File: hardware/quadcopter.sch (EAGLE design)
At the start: 92 parts, among them J1 HEADER-4POS-0.1IN-FEMALE-SMD-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, J2 HEADER-10POSTH-254X10, J3 HEADER-4POS-0.1IN-FEMALE, J4 AVR_SPI_PRG_6-SMD, M1 MOTOR_PADS_GND-MOLEX-SMD, M2 MOTOR_PADS_GND-MOLEX-SMD, M3 MOTOR_PADS_GND-MOLEX-SMD, M4 MOTOR_PADS_GND-MOLEX-SMD, Q1 N-MOSFET-SI2302DS, Q10 N-MOSFET-SI2302DS, Q11 N-MOSFET-SI2302DS, Q12 N-MOSFET-SI2302DS, Q2 N-MOSFET-SI2302DS, Q3 N-MOSFET-SI2302DS, Q4 N-MOSFET-SI2302DS, Q5 N-MOSFET-SI2302DS, Q6 N-MOSFET-SI2302DS, Q7 N-MOSFET-SI2302DS, Q8 N-MOSFET-SI2302DS, Q9 N-MOSFET-SI2302DS, SW1 PUSHBUTTON_-4.5X4.5, U1 ATMEGA128RFA1, U2 IMU_LSM9DS1-LSM9DS1, Y1 CRYSTAL5X3

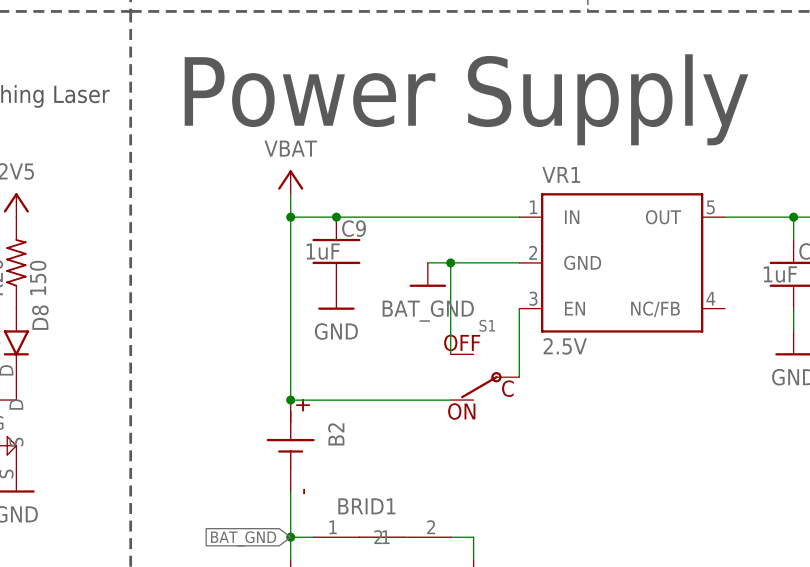
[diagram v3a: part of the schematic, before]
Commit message: Wire decoupling cap between VBAT and BAT_GND
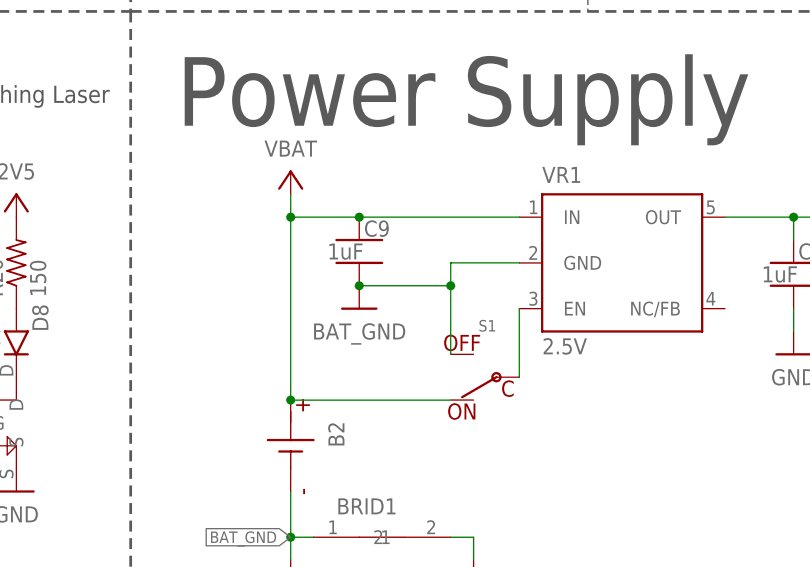
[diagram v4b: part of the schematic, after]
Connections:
- net BAT_GND: now also C9.2
- net GND: no longer C9.2
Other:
- moved on the sheet: C9
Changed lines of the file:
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@@
 <part name="C10" library="quadparts_prebuilt_2022" library_urn="urn:adsk.wipprod:fs.file:vf.VudH_-qgS-enOFMGlZoxrw" deviceset="CAPACITOR-NP_" device="SMD-2012-0805_CERAMIC-1UF" value="1uF"/>
 <part name="S1" library="quadparts_prebuilt_2022" library_urn="urn:adsk.wipprod:fs.file:vf.VudH_-qgS-enOFMGlZoxrw" deviceset="POWER-SWITCH-MFS201N-9-Z" device="-SMD-EDGE"/>
-<part name="GND31" library="quadparts_prebuilt_2022" library_urn="urn:adsk.wipprod:fs.file:vf.VudH_-qgS-enOFMGlZoxrw" deviceset="GND" device=""/>
 <part name="GND33" library="quadparts_prebuilt_2022" library_urn="urn:adsk.wipprod:fs.file:vf.VudH_-qgS-enOFMGlZoxrw" deviceset="GND" device=""/>
 <part name="GND32" library="quadparts_prebuilt_2022" library_urn="urn:adsk.wipprod:fs.file:vf.VudH_-qgS-enOFMGlZoxrw" deviceset="BAT_GND" device=""/>
@@
 <attribute name="NAME" x="373.38" y="110.49" size="1.778" layer="95"/>
 </instance>
-<instance part="C9" gate="G$1" x="350.52" y="104.14" smashed="yes">
-<attribute name="VALUE" x="346.964" y="101.981" size="1.778" layer="96"/>
-<attribute name="NAME" x="351.028" y="104.521" size="1.778" layer="95"/>
+<instance part="C9" gate="G$1" x="353.06" y="104.14" smashed="yes">
+<attribute name="VALUE" x="349.504" y="101.981" size="1.778" layer="96"/>
+<attribute name="NAME" x="353.568" y="104.521" size="1.778" layer="95"/>
 </instance>
 <instance part="C10" gate="G$1" x="401.32" y="101.6" smashed="yes">
@@
 <attribute name="NAME" x="368.3" y="95.25" size="1.27" layer="95" rot="R180"/>
 </instance>
-<instance part="GND31" gate="1" x="350.52" y="96.52" smashed="yes">
-<attribute name="VALUE" x="350.52" y="93.98" size="1.778" layer="96" align="center"/>
-</instance>
 <instance part="GND33" gate="1" x="365.76" y="66.04" smashed="yes">
 <attribute name="VALUE" x="365.76" y="63.5" size="1.778" layer="96" align="center"/>
@@
 <attribute name="VALUE" x="314.96" y="48.26" size="1.778" layer="96" rot="R180" align="center"/>
 </instance>
-<instance part="GND27" gate="1" x="360.68" y="99.06" smashed="yes">
-<attribute name="VALUE" x="360.68" y="96.52" size="1.778" layer="96" align="center"/>
+<instance part="GND27" gate="1" x="353.06" y="96.52" smashed="yes">
+<attribute name="VALUE" x="353.06" y="93.98" size="1.778" layer="96" align="center"/>
 </instance>
 <instance part="B1" gate="G$1" x="297.18" y="200.66" smashed="yes" rot="MR0">
@@
 </segment>
 <segment>
-<pinref part="C9" gate="G$1" pin="2"/>
-<pinref part="GND31" gate="1" pin="GND"/>
-</segment>
-<segment>
 <wire x1="363.22" y1="71.12" x2="365.76" y2="71.12" width="0.1524" layer="91"/>
 <wire x1="365.76" y1="71.12" x2="365.76" y2="68.58" width="0.1524" layer="91"/>
@@
 <segment>
 <wire x1="370.84" y1="101.6" x2="363.22" y2="101.6" width="0.1524" layer="91"/>
-<wire x1="363.22" y1="101.6" x2="360.68" y2="101.6" width="0.1524" layer="91"/>
+<wire x1="363.22" y1="99.06" x2="353.06" y2="99.06" width="0.1524" layer="91"/>
 <pinref part="VR1" gate="G$1" pin="GND"/>
 <pinref part="S1" gate="G$1" pin="OFF"/>
-<wire x1="363.22" y1="91.44" x2="363.22" y2="101.6" width="0.1524" layer="91"/>
+<wire x1="363.22" y1="91.44" x2="363.22" y2="99.06" width="0.1524" layer="91"/>
+<wire x1="363.22" y1="99.06" x2="363.22" y2="101.6" width="0.1524" layer="91"/>
 <pinref part="GND27" gate="1" pin="BAT_GND"/>
-<junction x="363.22" y="101.6"/>
+<pinref part="C9" gate="G$1" pin="2"/>
+<junction x="363.22" y="99.06"/>
+<junction x="353.06" y="99.06"/>
 </segment>
 </net>
@@
 <pinref part="B2" gate="G$1" pin="P"/>
 <pinref part="VR1" gate="G$1" pin="IN"/>
-<wire x1="370.84" y1="106.68" x2="350.52" y2="106.68" width="0.1524" layer="91"/>
+<wire x1="370.84" y1="106.68" x2="353.06" y2="106.68" width="0.1524" layer="91"/>
 <pinref part="C9" gate="G$1" pin="1"/>
-<wire x1="350.52" y1="106.68" x2="345.44" y2="106.68" width="0.1524" layer="91"/>
+<wire x1="353.06" y1="106.68" x2="345.44" y2="106.68" width="0.1524" layer="91"/>
 <junction x="345.44" y="86.36"/>
 <junction x="345.44" y="106.68"/>
-<junction x="350.52" y="106.68"/>
-</segment>
-<segment>
+<junction x="353.06" y="106.68"/>
+</segment>
+<segment>

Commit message: Modify IMU decoupling caps
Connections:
- removed net N$24: C13.2, U2.VDDIO
- removed net N$25: C14.1, C15.2
- removed net N$26: C14.2, U2.VDD
- net 2V5: now also C14.1, U2.VDD, U2.VDDIO
- net GND: now also C13.2, C14.2, C15.2
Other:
- moved on the sheet: C13, C14, C15
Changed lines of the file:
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@@
 <part name="GND27" library="quadparts_prebuilt_2022" library_urn="urn:adsk.wipprod:fs.file:vf.VudH_-qgS-enOFMGlZoxrw" deviceset="BAT_GND" device=""/>
 <part name="B1" library="quadparts_prebuilt_2022" library_urn="urn:adsk.wipprod:fs.file:vf.VudH_-qgS-enOFMGlZoxrw" deviceset="BALUN" device="0805"/>
+<part name="P+26" library="quadparts_prebuilt_2022" library_urn="urn:adsk.wipprod:fs.file:vf.VudH_-qgS-enOFMGlZoxrw" deviceset="2V5" device=""/>
+<part name="GND31" library="quadparts_prebuilt_2022" library_urn="urn:adsk.wipprod:fs.file:vf.VudH_-qgS-enOFMGlZoxrw" deviceset="GND" device=""/>
+<part name="P+27" library="quadparts_prebuilt_2022" library_urn="urn:adsk.wipprod:fs.file:vf.VudH_-qgS-enOFMGlZoxrw" deviceset="2V5" device=""/>
+<part name="P+28" library="quadparts_prebuilt_2022" library_urn="urn:adsk.wipprod:fs.file:vf.VudH_-qgS-enOFMGlZoxrw" deviceset="2V5" device=""/>
+<part name="GND53" library="quadparts_prebuilt_2022" library_urn="urn:adsk.wipprod:fs.file:vf.VudH_-qgS-enOFMGlZoxrw" deviceset="GND" device=""/>
+<part name="GND54" library="quadparts_prebuilt_2022" library_urn="urn:adsk.wipprod:fs.file:vf.VudH_-qgS-enOFMGlZoxrw" deviceset="GND" device=""/>
 </parts>
 <sheets>
@@
 <attribute name="VALUE" x="83.82" y="203.2" size="1.778" layer="96" align="center"/>
 </instance>
-<instance part="C13" gate="G$1" x="60.96" y="256.54" smashed="yes">
-<attribute name="VALUE" x="57.404" y="254.381" size="1.778" layer="96"/>
-<attribute name="NAME" x="61.468" y="256.921" size="1.778" layer="95"/>
-</instance>
-<instance part="C14" gate="G$1" x="43.18" y="256.54" smashed="yes">
-<attribute name="VALUE" x="39.624" y="254.381" size="1.778" layer="96"/>
-<attribute name="NAME" x="43.688" y="256.921" size="1.778" layer="95"/>
-</instance>
-<instance part="C15" gate="G$1" x="43.18" y="264.16" smashed="yes">
+<instance part="C13" gate="G$1" x="66.04" y="261.62" smashed="yes">
+<attribute name="VALUE" x="62.484" y="259.461" size="1.778" layer="96"/>
+<attribute name="NAME" x="66.548" y="262.001" size="1.778" layer="95"/>
+</instance>
+<instance part="C14" gate="G$1" x="43.18" y="264.16" smashed="yes">
 <attribute name="VALUE" x="39.624" y="262.001" size="1.778" layer="96"/>
 <attribute name="NAME" x="43.688" y="264.541" size="1.778" layer="95"/>
+</instance>
+<instance part="C15" gate="G$1" x="35.56" y="264.16" smashed="yes">
+<attribute name="VALUE" x="32.004" y="262.001" size="1.778" layer="96"/>
+<attribute name="NAME" x="36.068" y="264.541" size="1.778" layer="95"/>
 </instance>
 <instance part="C16" gate="G$1" x="73.66" y="210.82" smashed="yes">
@@
 <attribute name="VALUE" x="30.48" y="256.54" size="1.778" layer="96" rot="R180" align="center"/>
 </instance>
-<instance part="P+8" gate="G$1" x="43.18" y="269.24" smashed="yes">
-<attribute name="VALUE" x="43.18" y="271.78" size="1.778" layer="96" rot="R180" align="center"/>
-</instance>
-<instance part="P+10" gate="G$1" x="60.96" y="261.62" smashed="yes">
-<attribute name="VALUE" x="60.96" y="264.16" size="1.778" layer="96" rot="R180" align="center"/>
+<instance part="P+8" gate="G$1" x="50.8" y="261.62" smashed="yes">
+<attribute name="VALUE" x="50.8" y="264.16" size="1.778" layer="96" rot="R180" align="center"/>
+</instance>
+<instance part="P+10" gate="G$1" x="55.88" y="261.62" smashed="yes">
+<attribute name="VALUE" x="55.88" y="264.16" size="1.778" layer="96" rot="R180" align="center"/>
 </instance>
 <instance part="P+11" gate="G$1" x="83.82" y="223.52" smashed="yes">
@@
 <instance part="B1" gate="G$1" x="297.18" y="200.66" smashed="yes" rot="MR0">
 <attribute name="NAME" x="302.26" y="180.34" size="1.778" layer="95" rot="MR0"/>
+</instance>
+<instance part="P+26" gate="G$1" x="66.04" y="266.7" smashed="yes">
+<attribute name="VALUE" x="66.04" y="269.24" size="1.778" layer="96" rot="R180" align="center"/>
+</instance>
+<instance part="GND31" gate="1" x="66.04" y="254" smashed="yes">
+<attribute name="VALUE" x="66.04" y="251.46" size="1.778" layer="96" align="center"/>
+</instance>
+<instance part="P+27" gate="G$1" x="43.18" y="269.24" smashed="yes">
+<attribute name="VALUE" x="43.18" y="271.78" size="1.778" layer="96" rot="R180" align="center"/>
+</instance>
+<instance part="P+28" gate="G$1" x="35.56" y="269.24" smashed="yes">
+<attribute name="VALUE" x="35.56" y="271.78" size="1.778" layer="96" rot="R180" align="center"/>
+</instance>
+<instance part="GND53" gate="1" x="43.18" y="256.54" smashed="yes">
+<attribute name="VALUE" x="43.18" y="254" size="1.778" layer="96" align="center"/>
+</instance>
+<instance part="GND54" gate="1" x="35.56" y="256.54" smashed="yes">
+<attribute name="VALUE" x="35.56" y="254" size="1.778" layer="96" align="center"/>
 </instance>
 </instances>
@@
 <wire x1="254" y1="175.26" x2="251.46" y2="175.26" width="0.1524" layer="91"/>
 <label x="254" y="175.26" size="1.27" layer="95" xref="yes"/>
+</segment>
+<segment>
+<pinref part="C13" gate="G$1" pin="2"/>
+<pinref part="GND31" gate="1" pin="GND"/>
+</segment>
+<segment>
+<pinref part="C14" gate="G$1" pin="2"/>
+<pinref part="GND53" gate="1" pin="GND"/>
+</segment>
+<segment>
+<pinref part="C15" gate="G$1" pin="2"/>
+<pinref part="GND54" gate="1" pin="GND"/>
 </segment>
 </net>
@@
 <pinref part="R9" gate="G$1" pin="2"/>
 <pinref part="P+7" gate="G$1" pin="2V5"/>
-</segment>
-<segment>
-<pinref part="C15" gate="G$1" pin="1"/>
-<pinref part="P+8" gate="G$1" pin="2V5"/>
-</segment>
-<segment>
-<pinref part="C13" gate="G$1" pin="1"/>
-<pinref part="P+10" gate="G$1" pin="2V5"/>
 </segment>
 <segment>
@@
 <pinref part="P+21" gate="G$1" pin="2V5"/>
 </segment>
+<segment>
+<pinref part="U2" gate="G$1" pin="VDDIO"/>
+<pinref part="P+10" gate="G$1" pin="2V5"/>
+<wire x1="55.88" y1="259.08" x2="55.88" y2="251.46" width="0.1524" layer="91"/>
+</segment>
+<segment>
+<pinref part="C13" gate="G$1" pin="1"/>
+<pinref part="P+26" gate="G$1" pin="2V5"/>
+</segment>
+<segment>
+<pinref part="U2" gate="G$1" pin="VDD"/>
+<pinref part="P+8" gate="G$1" pin="2V5"/>
+<wire x1="50.8" y1="259.08" x2="50.8" y2="251.46" width="0.1524" layer="91"/>
+</segment>
+<segment>
+<pinref part="C14" gate="G$1" pin="1"/>
+<pinref part="P+27" gate="G$1" pin="2V5"/>
+</segment>
+<segment>
+<pinref part="C15" gate="G$1" pin="1"/>
+<pinref part="P+28" gate="G$1" pin="2V5"/>
+</segment>
 </net>
 <net name="PG0" class="0">
@@
 </segment>
 </net>
-<net name="N$24" class="0">
-<segment>
-<pinref part="C13" gate="G$1" pin="2"/>
-<wire x1="60.96" y1="251.46" x2="55.88" y2="251.46" width="0.1524" layer="91"/>
-<pinref part="U2" gate="G$1" pin="VDDIO"/>
-</segment>
-</net>
-<net name="N$25" class="0">
-<segment>
-<pinref part="C14" gate="G$1" pin="1"/>
-<pinref part="C15" gate="G$1" pin="2"/>
-</segment>
-</net>
-<net name="N$26" class="0">
-<segment>
-<pinref part="C14" gate="G$1" pin="2"/>
-<wire x1="43.18" y1="251.46" x2="50.8" y2="251.46" width="0.1524" layer="91"/>
-<pinref part="U2" gate="G$1" pin="VDD"/>
-</segment>
-</net>

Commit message: Swap C1 and CAP caps in IMU
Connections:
- net N$16: now also C12.1; no longer C16.1
- net N$22: now also C16.1; no longer C12.1
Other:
- moved on the sheet: C12, C16
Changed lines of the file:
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@@
 <attribute name="VALUE" x="55.88" y="195.58" size="1.778" layer="96" align="center"/>
 </instance>
-<instance part="C12" gate="G$1" x="83.82" y="213.36" smashed="yes">
-<attribute name="VALUE" x="80.264" y="211.201" size="1.778" layer="96"/>
-<attribute name="NAME" x="84.328" y="213.741" size="1.778" layer="95"/>
+<instance part="C12" gate="G$1" x="73.66" y="210.82" smashed="yes">
+<attribute name="VALUE" x="70.104" y="208.661" size="1.778" layer="96"/>
+<attribute name="NAME" x="74.168" y="211.201" size="1.778" layer="95"/>
 </instance>
 <instance part="GND35" gate="1" x="83.82" y="205.74" smashed="yes">
@@
 <attribute name="NAME" x="36.068" y="264.541" size="1.778" layer="95"/>
 </instance>
-<instance part="C16" gate="G$1" x="73.66" y="210.82" smashed="yes">
-<attribute name="VALUE" x="70.104" y="208.661" size="1.778" layer="96"/>
-<attribute name="NAME" x="74.168" y="211.201" size="1.778" layer="95"/>
+<instance part="C16" gate="G$1" x="83.82" y="213.36" smashed="yes">
+<attribute name="VALUE" x="80.264" y="211.201" size="1.778" layer="96"/>
+<attribute name="NAME" x="84.328" y="213.741" size="1.778" layer="95"/>
 </instance>
 <instance part="R9" gate="G$1" x="30.48" y="246.38" smashed="yes" rot="R90">
@@
 </segment>
 <segment>
-<pinref part="C12" gate="G$1" pin="2"/>
-<pinref part="GND35" gate="1" pin="GND"/>
-</segment>
-<segment>
 <pinref part="J2" gate="G$1" pin="7"/>
 <wire x1="63.5" y1="137.16" x2="66.04" y2="137.16" width="0.1524" layer="91"/>
@@
 <wire x1="60.96" y1="165.1" x2="63.5" y2="165.1" width="0.1524" layer="91"/>
 <label x="63.5" y="165.1" size="1.27" layer="95" xref="yes"/>
-</segment>
-<segment>
-<pinref part="C16" gate="G$1" pin="2"/>
-<pinref part="GND37" gate="1" pin="GND"/>
 </segment>
 <segment>
@@
 <pinref part="C15" gate="G$1" pin="2"/>
 <pinref part="GND54" gate="1" pin="GND"/>
+</segment>
+<segment>
+<pinref part="GND37" gate="1" pin="GND"/>
+<pinref part="C12" gate="G$1" pin="2"/>
+</segment>
+<segment>
+<pinref part="GND35" gate="1" pin="GND"/>
+<pinref part="C16" gate="G$1" pin="2"/>
 </segment>
 </net>
@@
 </segment>
 </net>
-<net name="N$22" class="0">
-<segment>
-<wire x1="73.66" y1="215.9" x2="83.82" y2="215.9" width="0.1524" layer="91"/>
-<pinref part="C12" gate="G$1" pin="1"/>
-<pinref part="U2" gate="G$1" pin="C1"/>
-</segment>
-</net>
 <net name="TX0" class="0">
 <segment>
@@
 </segment>
 </net>
-<net name="N$16" class="0">
-<segment>
-<pinref part="C16" gate="G$1" pin="1"/>
-<pinref part="U2" gate="G$1" pin="CAP"/>
-</segment>
-</net>
 <net name="PWM5" class="0">
 <segment>
@@
 </segment>
 </net>
+<net name="N$16" class="0">
+<segment>
+<pinref part="U2" gate="G$1" pin="CAP"/>
+<pinref part="C12" gate="G$1" pin="1"/>
+</segment>
+</net>
+<net name="N$22" class="0">
+<segment>
+<pinref part="C16" gate="G$1" pin="1"/>
+<wire x1="83.82" y1="215.9" x2="73.66" y2="215.9" width="0.1524" layer="91"/>
+<pinref part="U2" gate="G$1" pin="C1"/>
+</segment>
+</net>

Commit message: Replaced `-SMD` variant battery with `-SMD-TH` variant
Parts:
- B2: value BATTERY-SMD -> BATTERY-SMD-TH; device quadparts_prebuilt_2022:BATTERY-SMD -> quadparts_prebuilt_2022:BATTERY-SMD-TH
